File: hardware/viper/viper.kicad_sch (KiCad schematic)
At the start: 52 parts, among them J1 TYPE-C-31-M-12, Q1 2N7002, U1 ATmega32U4-A, U2 USBLC6-2SC6, Y1 16MHz

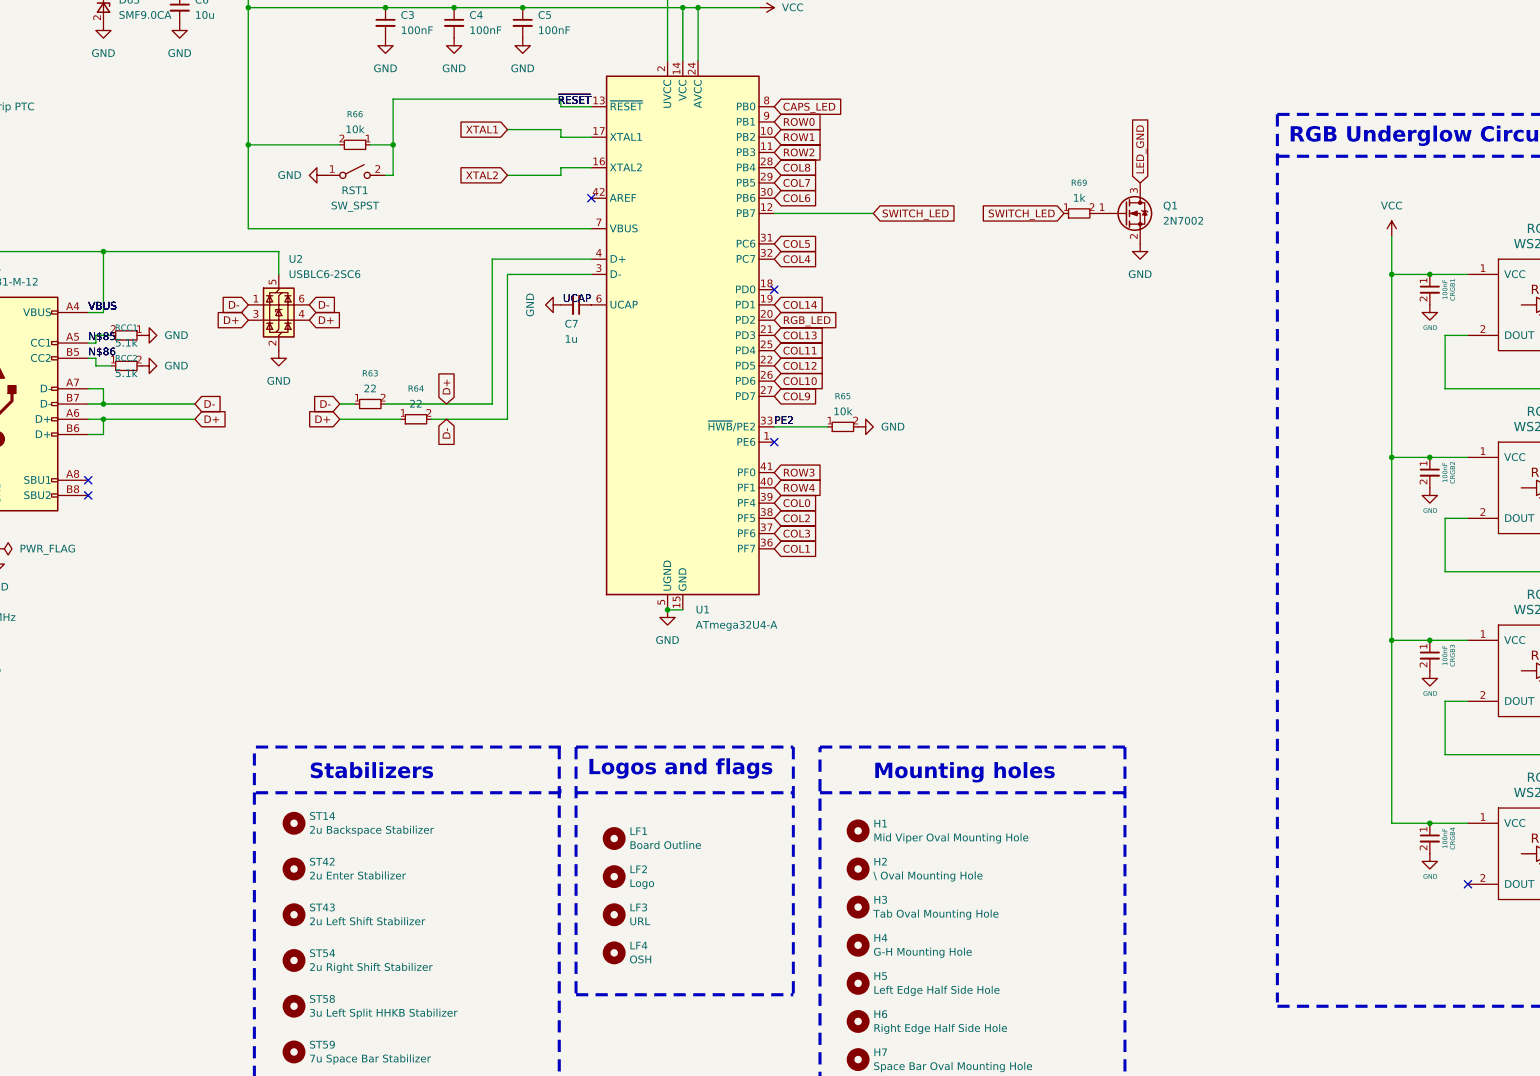
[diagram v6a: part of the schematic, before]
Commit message: Reannotated IC/USB resistors
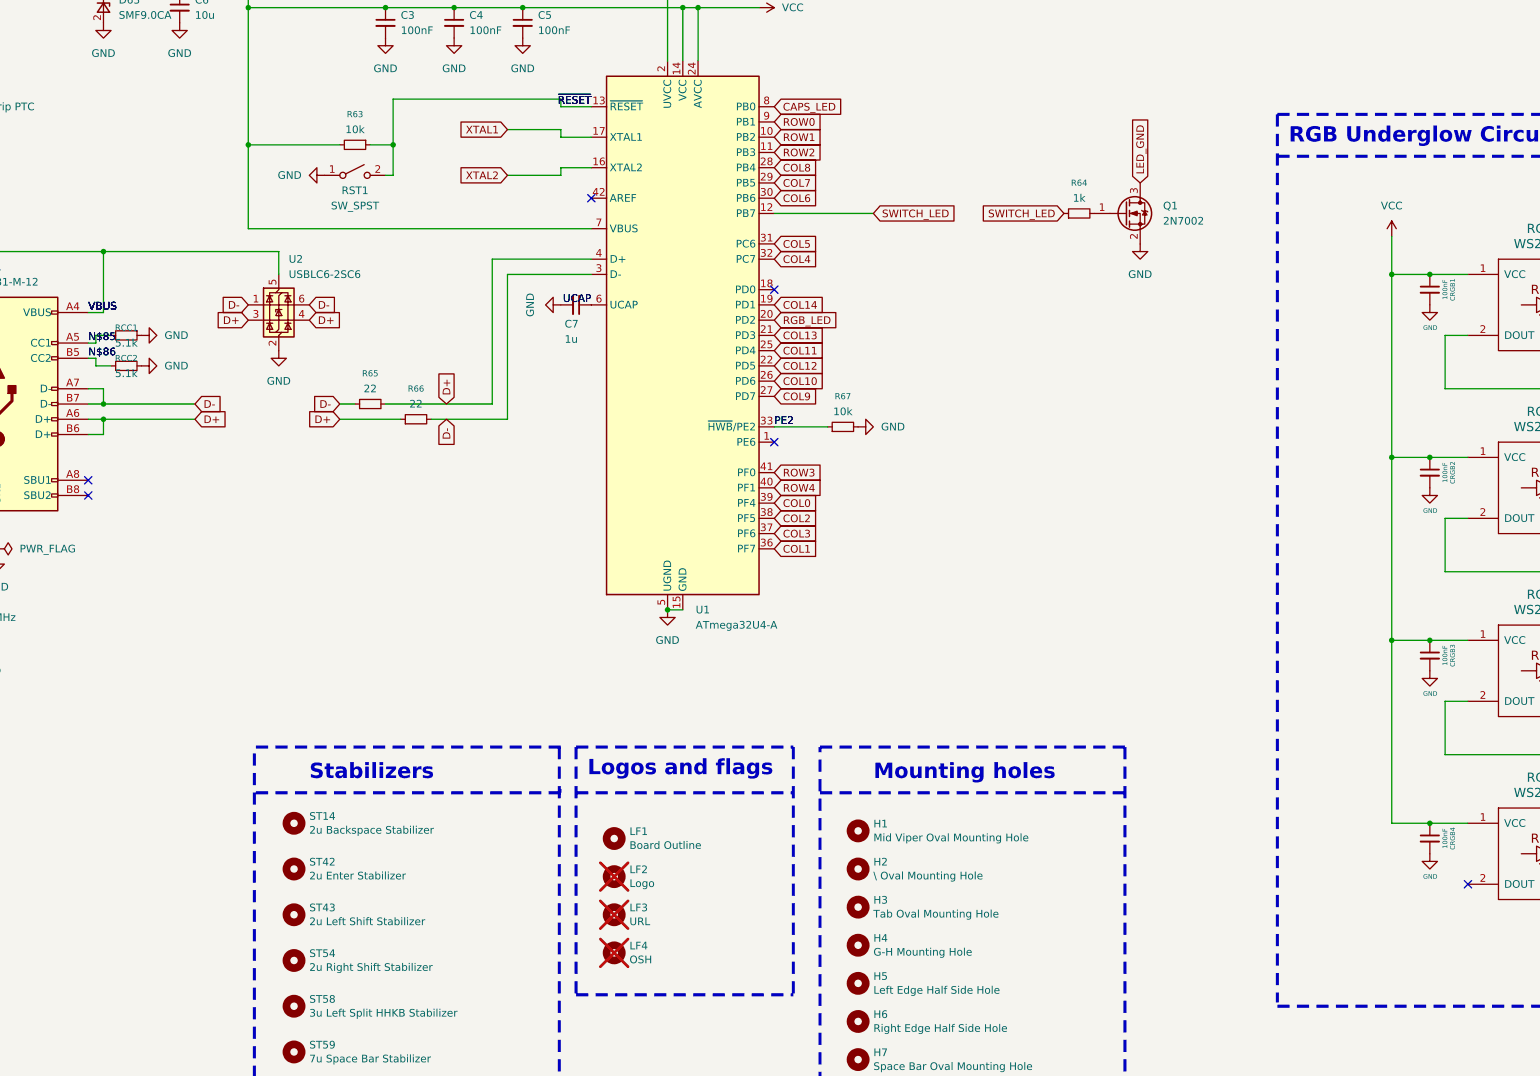
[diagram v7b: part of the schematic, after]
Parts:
- LF2, LF3, LF4: now not fitted
- renumbered R66 to R63, R69 to R64, R63 to R65, R64 to R66, R65 to R67
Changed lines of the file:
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@@
 	)
 	(symbol
+		(lib_name "GND_2")
 		(lib_id "power:GND")
 		(at 342.9 130.81 0)
@@
 		(in_bom no)
 		(on_board no)
-		(dnp no)
+		(dnp yes)
 		(property "Reference" "LF2"
 			(at 209.55 224.8916 0)
@@
 		(dnp no)
 		(fields_autoplaced yes)
-		(property "Reference" "R66"
+		(property "Reference" "R63"
 			(at 163.83 99.06 90)
 			(effects
@@
 			(project "viper"
 				(path "/9e45a776-7007-48ff-b543-dc98423173b7"
-					(reference "R66")
+					(reference "R63")
 					(unit 1)
 				)
@@
 	)
 	(symbol
+		(lib_name "C_Small_5")
 		(lib_id "Device:C_Small")
 		(at 342.9 219.71 0)
@@
 		(dnp no)
 		(fields_autoplaced yes)
-		(property "Reference" "R64"
+		(property "Reference" "R66"
 			(at 173.99 144.78 90)
 			(effects
@@
 			(project "viper"
 				(path "/9e45a776-7007-48ff-b543-dc98423173b7"
-					(reference "R64")
+					(reference "R66")
 					(unit 1)
 				)
@@
 	)
 	(symbol
+		(lib_name "GND_4")
 		(lib_id "power:GND")
 		(at 342.9 222.25 0)
@@
 	)
 	(symbol
+		(lib_name "GND_5")
 		(lib_id "power:GND")
 		(at 342.9 161.29 0)
@@
 	)
 	(symbol
+		(lib_name "C_Small_8")
 		(lib_id "Device:C_Small")
 		(at 342.9 128.27 0)
@@
 	)
 	(symbol
+		(lib_name "C_Small_9")
 		(lib_id "Device:C_Small")
 		(at 342.9 189.23 0)
@@
 		(on_board yes)
 		(dnp no)
-		(property "Reference" "R63"
+		(property "Reference" "R65"
 			(at 166.37 142.24 90)
 			(effects
@@
 			(project "viper"
 				(path "/9e45a776-7007-48ff-b543-dc98423173b7"
-					(reference "R63")
+					(reference "R65")
 					(unit 1)
 				)
@@
 	)
 	(symbol
+		(lib_name "GND_6")
 		(lib_id "power:GND")
 		(at 342.9 191.77 0)
@@
 	)
 	(symbol
-		(lib_name "R_Small_1")
+		(lib_name "R_Small_6")
 		(lib_id "Device:R_Small")
 		(at 284.48 115.57 90)
@@
 		(dnp no)
 		(fields_autoplaced yes)
-		(property "Reference" "R69"
+		(property "Reference" "R64"
 			(at 284.48 110.49 90)
 			(effects
@@
 			(project "viper"
 				(path "/9e45a776-7007-48ff-b543-dc98423173b7"
-					(reference "R69")
+					(reference "R64")
 					(unit 1)
 				)
@@
 		(in_bom no)
 		(on_board no)
-		(dnp no)
+		(dnp yes)
 		(property "Reference" "LF4"
 			(at 209.55 237.5916 0)
@@
 		(in_bom no)
 		(on_board no)
-		(dnp no)
+		(dnp yes)
 		(property "Reference" "LF3"
 			(at 209.55 231.2416 0)
@@
 		(dnp no)
 		(fields_autoplaced yes)
-		(property "Reference" "R65"
+		(property "Reference" "R67"
 			(at 245.11 146.05 90)
 			(effects
@@
 			(project "viper"
 				(path "/9e45a776-7007-48ff-b543-dc98423173b7"
-					(reference "R65")
+					(reference "R67")
 					(unit 1)
 				)

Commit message: Improved schematic
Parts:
- H1: value Mid Viper Oval Mounting Hole -> ~
- H2: value \ Oval Mounting Hole -> ~
- H3: value Tab Oval Mounting Hole -> ~
- H4: value G-H Mounting Hole -> ~
- H5: value Left Edge Half Side Hole -> ~
- H6: value Right Edge Half Side Hole -> ~
- H7: value Space Bar Oval Mounting Hole -> ~
- H8: value Left Bottom Half Side Hole -> ~
- H9: value Right Bottom Half Side Hole -> ~
- LF1: value Board Outline -> ~
- LF2: value Logo -> ~
- LF3: value URL -> ~
- LF4: value OSH -> ~
- RGB1, RGB2, RGB3, RGB4: footprint locallib:LED_SMD3528-4P-WS2812B -> LED_SMD:LED_WS2812B_PLCC4_5.0x5.0mm_P3.2mm; symbol ws2812b:WS2812B -> LED:WS2812B
- ST14: value 2u Backspace Stabilizer -> ~
- ST42: value 2u Enter Stabilizer -> ~
- ST43: value 2u Left Shift Stabilizer -> ~
- ST54: value 2u Right Shift Stabilizer -> ~
- ST58, ST60: value 3u Left Split HHKB Stabilizer -> ~
- ST59: value 7u Space Bar Stabilizer -> ~
- ST59_1: value 8u Space Bar Stabilizer -> ~
- U1: value ATmega32U4-A -> ATmega32U4-M; symbol MCU_Microchip_ATmega:ATmega32U4-A -> MCU_Microchip_ATmega:ATmega32U4-M
- renumbered C2 to C1, C1 to C2, C4 to C3, C3 to C4
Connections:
- net D+: no longer R65.2, R66.1, U1.4 (D+), U2.4 (I/O2)
- net D-: no longer R65.1, R66.2, U1.3 (D-), U2.6 (I/O1)
- net GND: now also U1.45 (GND)
- net N$85: no longer names the net of J1.A5 (CC1), RCC1.2
- net N$86: no longer names the net of J1.B5 (CC2), RCC2.1
- net PE2: no longer names the net of R67.1, U1.33 (~{HWB}/PE2)
- net SWITCH_LED: no longer names the net of R64.1, U1.12 (PB7)
- net UCAP: no longer names the net of C7.1, U1.6 (UCAP)
- new net u2/mcu/D+: R65.1, R65.2, U1.4 (D+), U2.4 (I/O2)
- new net u2/mcu/D-: R66.1, R66.2, U1.3 (D-), U2.6 (I/O1)
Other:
- note added: "Clock circuit"
- note added: "EMI (?)"
- note added: "Hard reset circuit"
- note added: "Microcontroller"
- note added: "Power Supply & Protection"
- note added: "USB Connector"
- note added: "USB ESD"
- moved on the sheet: C3, C4, C5, C6, C7, CRGB1, CRGB2, CRGB3, CRGB4, D63, F1, H1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
